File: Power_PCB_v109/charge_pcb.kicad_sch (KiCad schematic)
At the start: 48 parts, among them J1 Mow3, J10 Mot_Left, J11 DC/DC1, J12 DC/DC2, J2 Main_PCB1, J3 Mow2, J4 Battery, J5 Main_PCB2, J6 Power Switch, J7 Mow1, J8 Mot_Right, J9 Start, Q1 BC547C, Q2 IRF9540N, Q3 BC547C, Q4 IRF9540N, U1 INA226, U2 INA226, U3 INA Charge, U4 INA226, U5 INA226, U6 INA226

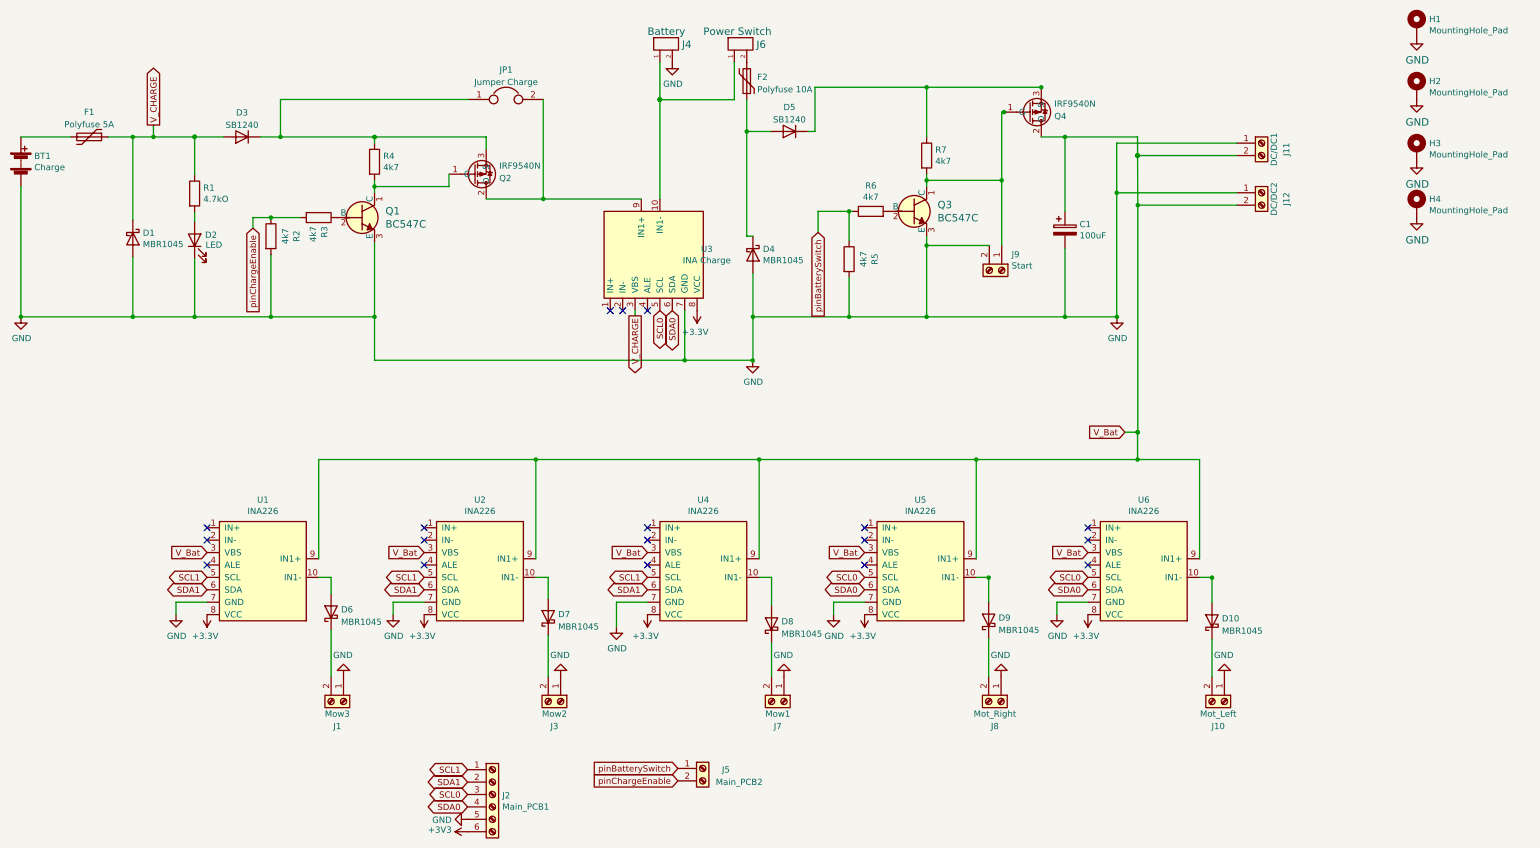
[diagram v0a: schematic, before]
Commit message: Change SDA SCL Footprint
Ad new Schematic PDF and BOOM File
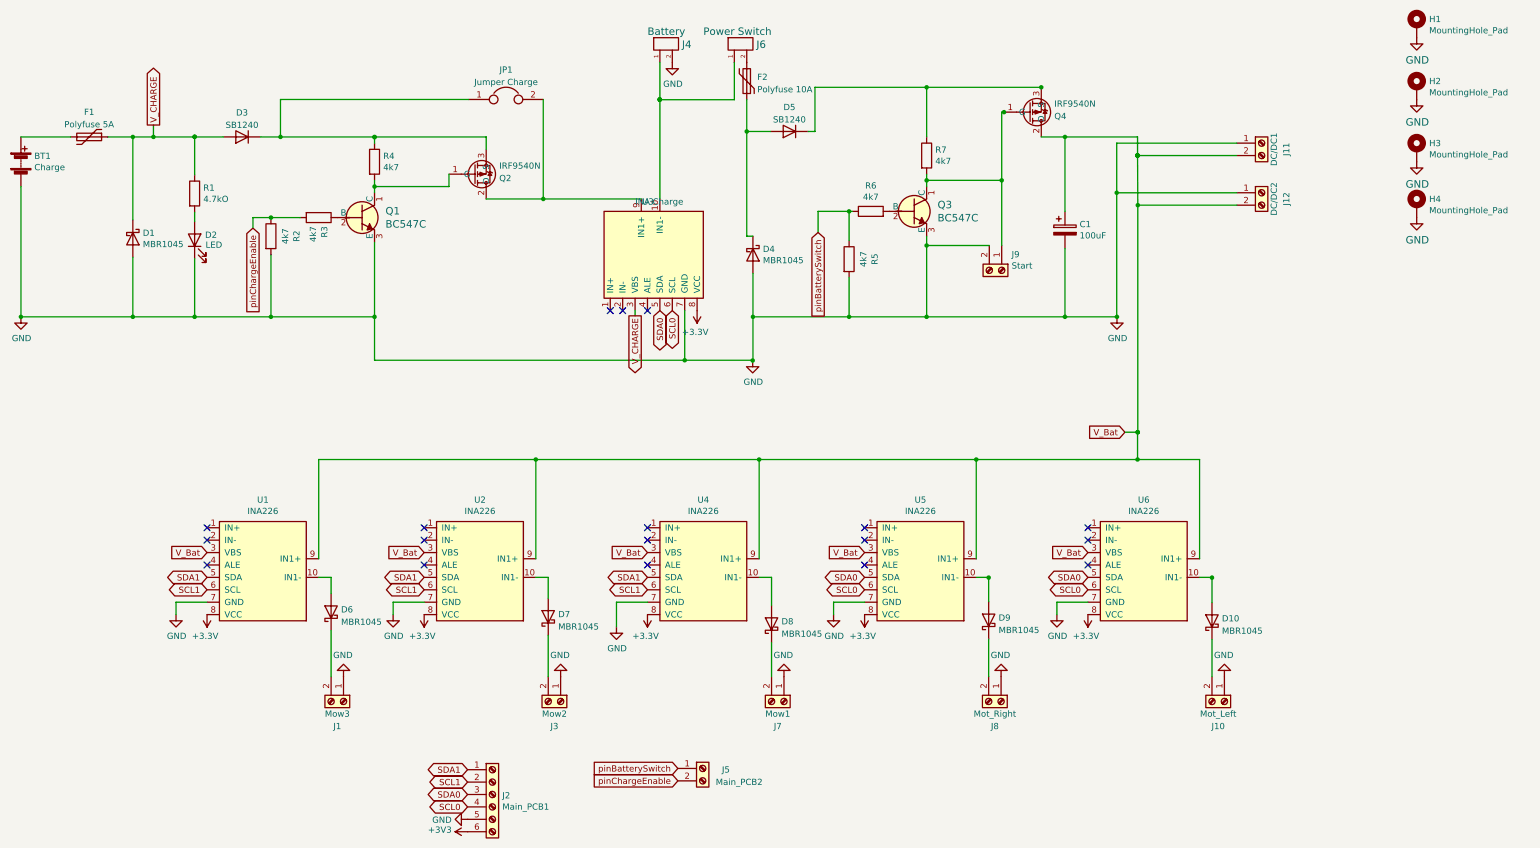
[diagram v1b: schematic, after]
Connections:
- net SCL0: now also J2.4 (Pin_4), U3.6 (SCL), U5.6 (SCL), U6.6 (SCL); no longer J2.3 (Pin_3), U3.5 (SCL), U5.5 (SCL), U6.5 (SCL)
- net SCL1: now also J2.2 (Pin_2), U1.6 (SCL), U2.6 (SCL), U4.6 (SCL); no longer J2.1 (Pin_1), U1.5 (SCL), U2.5 (SCL), U4.5 (SCL)
- net SDA0: now also J2.3 (Pin_3), U3.5 (SDA), U5.5 (SDA), U6.5 (SDA); no longer J2.4 (Pin_4), U3.6 (SDA), U5.6 (SDA), U6.6 (SDA)
- net SDA1: now also J2.1 (Pin_1), U1.5 (SDA), U2.5 (SDA), U4.5 (SDA); no longer J2.2 (Pin_2), U1.6 (SDA), U2.6 (SDA), U4.6 (SDA)
